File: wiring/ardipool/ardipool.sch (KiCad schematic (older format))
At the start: 23 parts, among them K1 filter, K2 ph, P1 Digital, P10 CONN_01X01, P11 CONN_01X01, P12 CONN_01X01, P13 CONN_01X01, P2 Power, P3 Analog, P4 Analog, P5 PWM, P6 PWM, P7 Communication, P8 CONN_01X01, P9 CONN_01X01, SW1 SW_Push_Dual, U1 DS18B20, U2 DS18B20, U3 DHT11, U4 DS1307+

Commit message: schem
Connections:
- net 6(**) is gone; now on net LCD5: P6.2 (Pin_2)
- net 7(**) is gone; now on net LCD4: P6.1 (Pin_1)
- net LCD4: no longer P6.3 (Pin_3)
- net LCD5: no longer P6.4 (Pin_4)
- net LCD6: now also P6.3 (Pin_3); no longer P6.5 (Pin_5)
- net LCD7: now also P6.4 (Pin_4); no longer P6.6 (Pin_6)
- net 18(Tx1) renamed Rotary2
- net 19(Rx1) renamed Rotary1
- new net 3(**): P6.5 (Pin_5)
- new net RotaryB: P6.6 (Pin_6)
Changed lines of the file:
@@
 	8900 3150 9350 3150
 Wire Wire Line
-	10400 2450 10150 2450
-Wire Wire Line
-	10150 2550 10400 2550
-Wire Wire Line
 	10400 3050 10150 3050
 Wire Wire Line
@@
 Wire Wire Line
 	10150 3700 10400 3700
-Wire Wire Line
-	10400 3800 10150 3800
-Wire Wire Line
-	10150 3900 10400 3900
-Wire Wire Line
-	10400 4000 10150 4000
-Wire Wire Line
-	10150 4100 10400 4100
 Wire Wire Line
 	10500 4850 10500 4650
@@
 	1    0    0    -1
 $EndComp
-Text GLabel 10400 4000 2    50   Input ~ 0
+Text GLabel 10850 4000 2    50   Input ~ 0
 SDA
-Text GLabel 10400 4100 2    50   Input ~ 0
+Text GLabel 10850 4100 2    50   Input ~ 0
 SCL
 Wire Wire Line
@@
 Wire Wire Line
 	6050 5850 6300 5850
-Text GLabel 10700 2650 2    50   Input ~ 0
+Text GLabel 10850 2450 2    50   Input ~ 0
 LCD4
-Text GLabel 10700 2750 2    50   Input ~ 0
+Text GLabel 10850 2550 2    50   Input ~ 0
 LCD5
-Text GLabel 10700 2850 2    50   Input ~ 0
+Text GLabel 10850 2650 2    50   Input ~ 0
 LCD6
-Text GLabel 10700 2950 2    50   Input ~ 0
+Text GLabel 10850 2750 2    50   Input ~ 0
 LCD7
 Wire Wire Line
-	10150 2650 10700 2650
-Wire Wire Line
-	10150 2750 10700 2750
-Wire Wire Line
 	10150 2850 10700 2850
-Wire Wire Line
-	10150 2950 10700 2950
 Text GLabel 10850 1650 2    50   Input ~ 0
 LCDRS
@@
 Wire Wire Line
 	3250 4000 3250 3900
+Wire Wire Line
+	10150 2450 10850 2450
+Wire Wire Line
+	10150 2550 10850 2550
+Wire Wire Line
+	10150 2650 10850 2650
+Wire Wire Line
+	10150 2750 10850 2750
+Wire Wire Line
+	10150 4000 10850 4000
+Wire Wire Line
+	10150 4100 10850 4100
+Text GLabel 10850 3900 2    50   Input ~ 0
+Rotary1
+Text GLabel 10850 3800 2    50   Input ~ 0
+Rotary2
+Text GLabel 10850 2950 2    50   Input ~ 0
+RotaryB
+Wire Wire Line
+	10150 2950 10850 2950
+Wire Wire Line
+	10150 3800 10850 3800
+Wire Wire Line
+	10150 3900 10850 3900
 $EndSCHEMATC

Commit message: update network
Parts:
- added U?: devkitC, symbol arduitouch:devkitC
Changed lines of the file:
@@
 Wire Wire Line
 	10150 3900 10850 3900
+Text GLabel 1350 950  0    50   Input ~ 0
+12V
+Text GLabel 1350 1100 0    50   Input ~ 0
+GND
+Text GLabel 1350 1250 0    50   Input ~ 0
+Relay1
+Text GLabel 1350 1400 0    50   Input ~ 0
+Relay2
+Text GLabel 1350 1550 0    50   Input ~ 0
+Relay3
+Text GLabel 1350 1700 0    50   Input ~ 0
+Relay3
+Text GLabel 1350 1850 0    50   Input ~ 0
+DS18B20
+Text GLabel 1350 800  0    50   Input ~ 0
+3.3V
+Text GLabel 1350 2000 0    50   Input ~ 0
+SCA
+Text GLabel 1350 2150 0    50   Input ~ 0
+SCL
+$Comp
+L arduitouch:devkitC U?
+U 1 1 5F01B682
+P 2650 1150
+F 0 "U?" H 3269 826 50  0000 L CNN
+F 1 "devkitC" H 3269 735 50  0000 L CNN
+F 2 "" H 2650 1150 50  0001 C CNN
+F 3 "" H 2650 1150 50  0001 C CNN
+	1    2650 1150
+	1    0    0    -1
+$EndComp
 $EndSCHEMATC

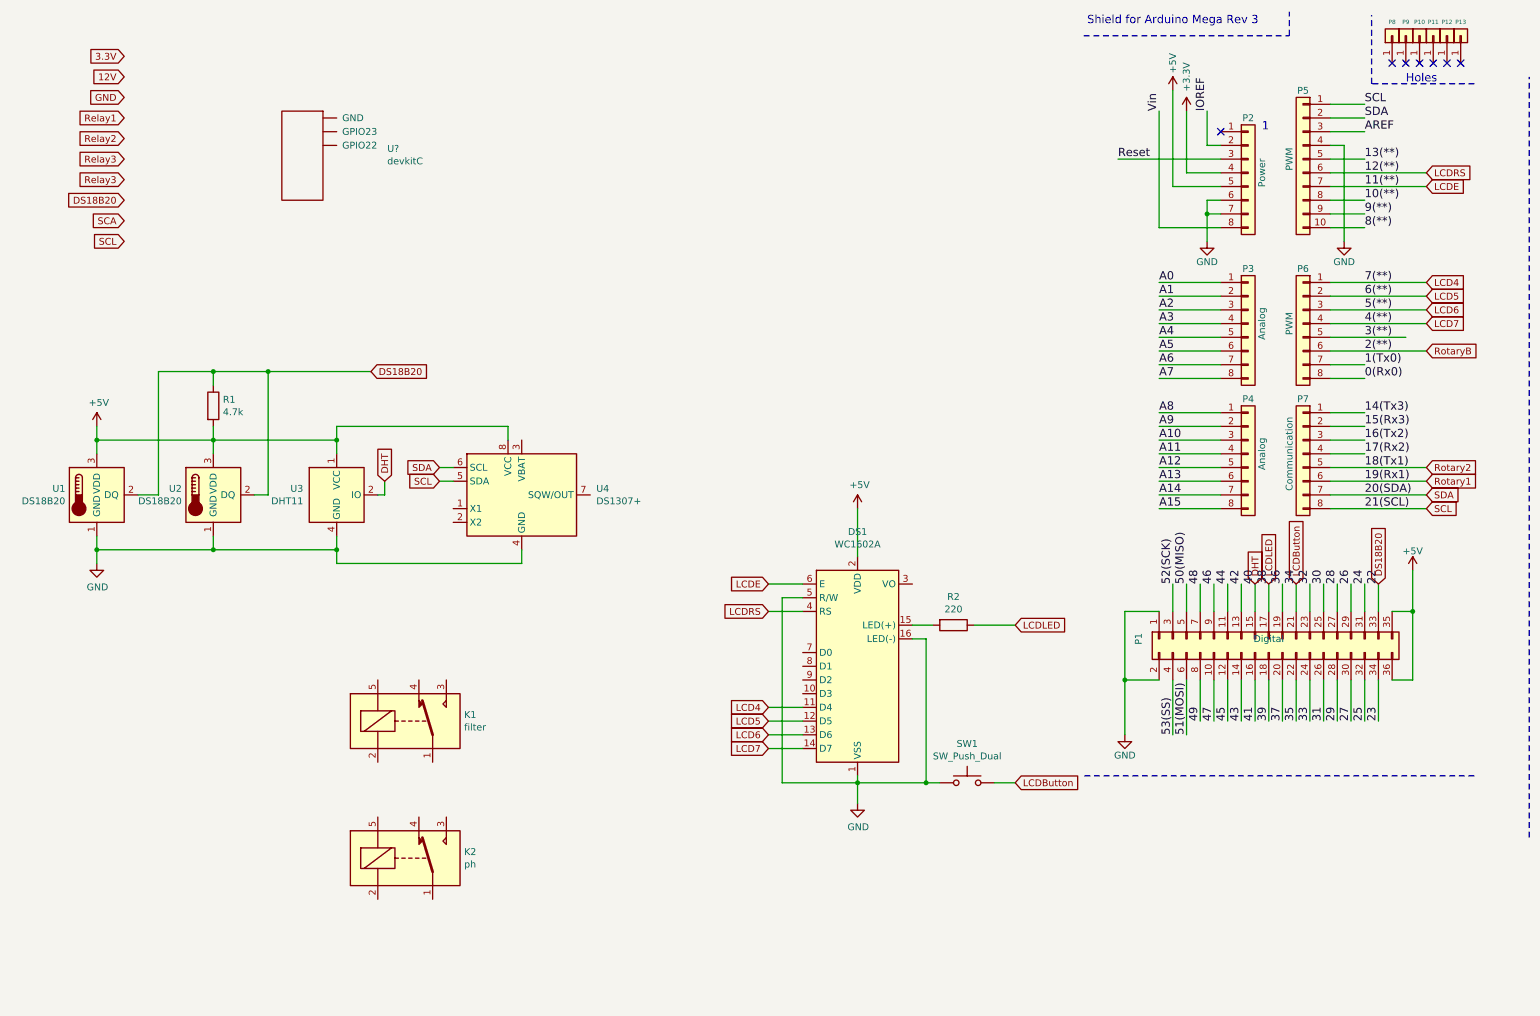
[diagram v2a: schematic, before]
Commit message: make use of config.states
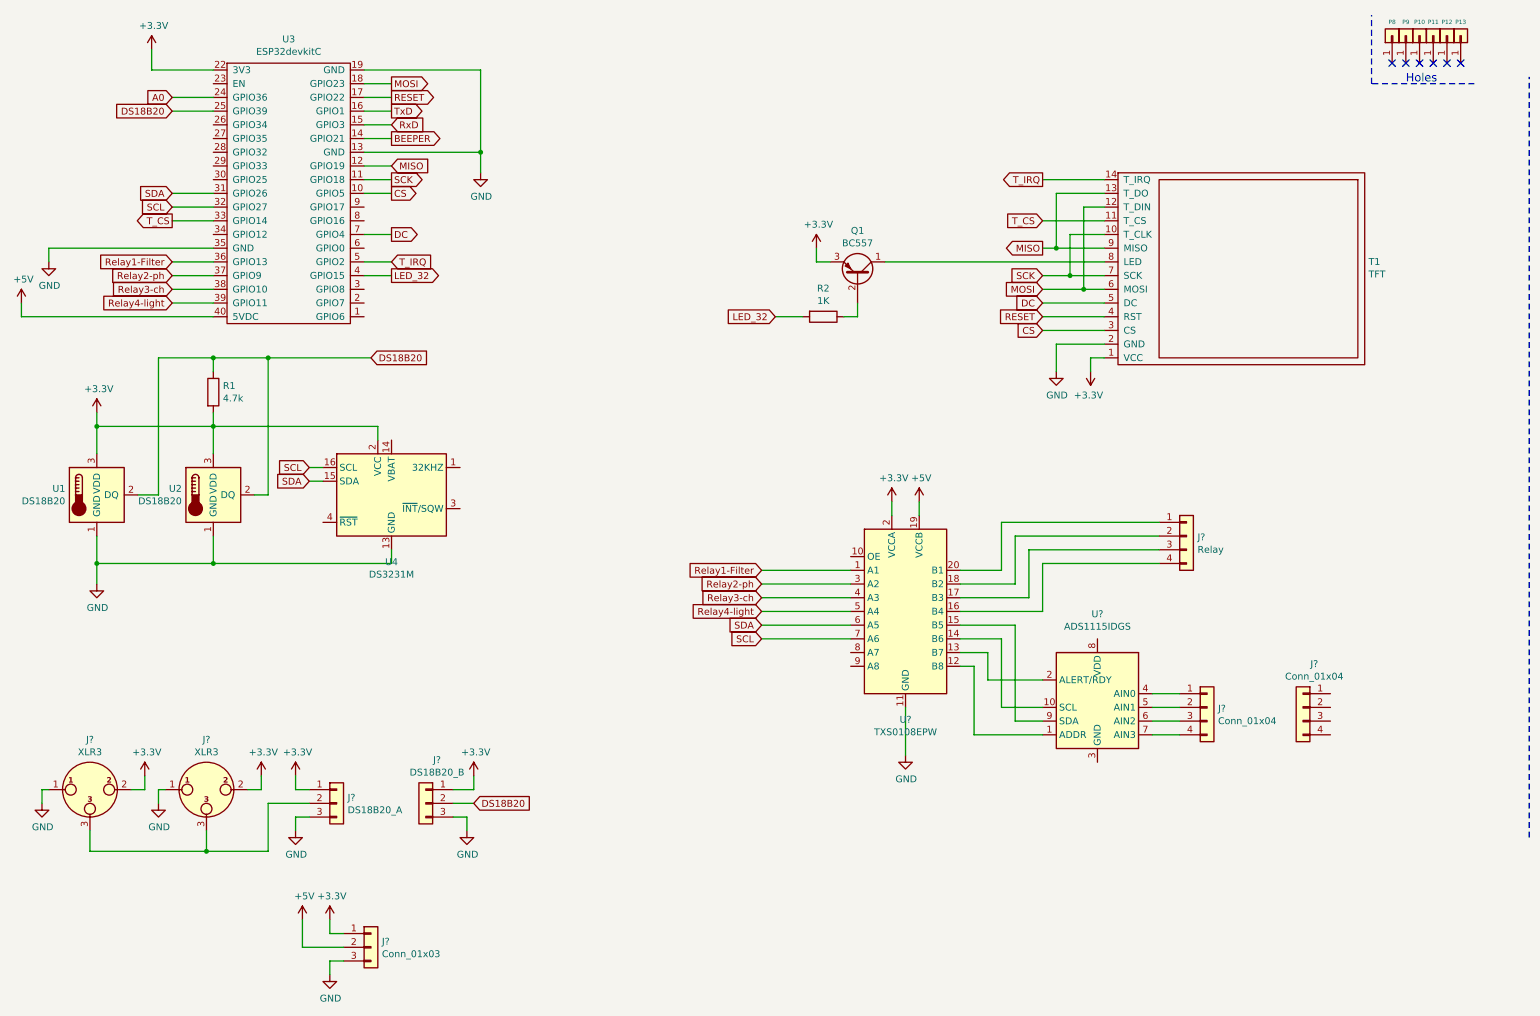
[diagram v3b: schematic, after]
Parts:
- removed DS1: WC1602A, Display:WC1602A, symbol Display_Character:WC1602A
- removed K1: filter, Relay_THT:Relay_SPDT_SANYOU_SRD_Series_Form_C, symbol Relay:SANYOU_SRD_Form_C
- removed K2: ph, Relay_THT:Relay_SPDT_SANYOU_SRD_Series_Form_C, symbol Relay:SANYOU_SRD_Form_C
- removed P1: Digital, Socket_Arduino_Mega:Socket_Strip_Arduino_2x18, symbol Connector_Generic:Conn_02x18_Odd_Even
- removed P2: Power, Socket_Arduino_Mega:Socket_Strip_Arduino_1x08, symbol Connector_Generic:Conn_01x08
- removed P3, P4: Analog, Socket_Arduino_Mega:Socket_Strip_Arduino_1x08, symbol Connector_Generic:Conn_01x08
- removed P5: PWM, Socket_Arduino_Mega:Socket_Strip_Arduino_1x10, symbol Connector_Generic:Conn_01x10
- removed P6: PWM, Socket_Arduino_Mega:Socket_Strip_Arduino_1x08, symbol Connector_Generic:Conn_01x08
- removed P7: Communication, Socket_Arduino_Mega:Socket_Strip_Arduino_1x08, symbol Connector_Generic:Conn_01x08
- removed SW1: SW_Push_Dual, Button_Switch_THT:SW_PUSH_6mm_H5mm, symbol Switch:SW_Push
- removed U3: DHT11, Sensor:Aosong_DHT11_5.5x12.0_P2.54mm, symbol Sensor:DHT11
- removed U4: DS1307+, Package_DIP:DIP-8_W7.62mm, symbol Timer_RTC:DS1307+
- removed U?: devkitC, symbol arduitouch:devkitC
- added J? (x2): XLR3, symbol Connector:XLR3
- added J?: Relay, symbol Connector_Generic:Conn_01x04
- added J? (x2): Conn_01x04, symbol Connector_Generic:Conn_01x04
- added J?: DS18B20_A, symbol Connector_Generic:Conn_01x03
- added J?: Conn_01x03, symbol Connector_Generic:Conn_01x03
- added J?: DS18B20_B, symbol Connector_Generic:Conn_01x03
- added Q1: BC557, Package_TO_SOT_THT:TO-92_Inline_Wide, symbol Transistor_BJT:BC557
- added T1: TFT, symbol arduitouch:TFT
- added U3: ESP32devkitC, symbol arduitouch:ESP32devkitC
- added U4: DS3231M, Package_SO:SOIC-16W_7.5x10.3mm_P1.27mm, symbol Timer_RTC:DS3231M
- added U?: TXS0108EPW, Package_SO:TSSOP-20_4.4x6.5mm_P0.65mm, symbol Logic_LevelTranslator:TXS0108EPW
- added U?: ADS1115IDGS, Package_SO:TSSOP-10_3x3mm_P0.5mm, symbol Analog_ADC:ADS1115IDGS
- R2: value 220 -> 1K; footprint Resistor_THT:R_Axial_DIN0207_L6.3mm_D2.5mm_P10.16mm_Horizontal -> (none)
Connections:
- net +3V3: now also R1.2, U1.3 (VDD), U2.3 (VDD), J?.1 (Pin_1), J?.1 (Pin_1), J?.1 (Pin_1), J?.2, J?.2, Q1.3 (E), T1.1 (VCC), U3.22 (3V3), U4.2 (VCC), U?.2 (VCCA)
- net +5V: now also J?.2 (Pin_2), U3.40 (5VDC), U?.19 (VCCB); no longer R1.2, U1.3 (VDD), U2.3 (VDD)
- net A0: now also U3.24 (GPIO36)
- net DS18B20: now also J?.2 (Pin_2), U3.25 (GPIO39)
- net GND: now also J?.1, J?.1, J?.3 (Pin_3), J?.3 (Pin_3), J?.3 (Pin_3), T1.2 (GND), U3.13 (GND), U3.19 (GND), U3.35 (GND), U4.10 (GND), U4.11 (GND), U4.12 (GND), U4.13 (GND), U4.5 (GND), U4.6 (GND), U4.7 (GND), U4.8 (GND), U4.9 (GND), U?.11 (GND)
- net SCL: now also U3.32 (GPIO27), U4.16 (SCL), U?.7 (A6)
- net SDA: now also U3.31 (GPIO26), U4.15 (SDA), U?.6 (A5)
- net LED_32: now reaches R2.2
- net LED_32: now also U3.4 (GPIO15)
- net LCDLED: no longer names the net of R2.1
- net LCDLED: now also Q1.2 (B)
- new net: Q1.1 (C), T1.8 (LED)
- new net: J?.2 (Pin_2), J?.3, J?.3
- new net: J?.1 (Pin_1), U?.20 (B1)
- new net: J?.2 (Pin_2), U?.18 (B2)
- new net: J?.3 (Pin_3), U?.17 (B3)
- new net: J?.4 (Pin_4), U?.16 (B4)
- new net: J?.1 (Pin_1), U?.4 (AIN0)
- new net: J?.2 (Pin_2), U?.5 (AIN1)
- new net: J?.3 (Pin_3), U?.6 (AIN2)
- new net: J?.4 (Pin_4), U?.7 (AIN3)
- new net: U?.1 (ADDR), U?.12 (B8)
- new net: U?.13 (B7), U?.2 (ALERT/RDY)
- new net: U?.10 (SCL), U?.14 (B6)
- new net: U?.15 (B5), U?.9 (SDA)
- new net BEEPER: U3.14 (GPIO21)
- new net CS: T1.3 (CS), U3.10 (GPIO5)
- new net DC: T1.5 (DC), U3.7 (GPIO4)
- new net MISO: T1.13 (T_DO), T1.9 (MISO), U3.12 (GPIO19)
- new net MOSI: T1.12 (T_DIN), T1.6 (MOSI), U3.18 (GPIO23)
- new net RESET: T1.4 (RST), U3.17 (GPIO22)
- new net Relay1-Filter: U3.36 (GPIO13), U?.1 (A1)
- new net Relay2-ph: U3.37 (GPIO9), U?.3 (A2)
- new net Relay3-ch: U3.38 (GPIO10), U?.4 (A3)
- new net Relay4-light: U3.39 (GPIO11), U?.5 (A4)
- new net RxD: U3.15 (GPIO3)
- new net SCK: T1.10 (T_CLK), T1.7 (SCK), U3.11 (GPIO18)
- new net T_CS: T1.11 (T_CS), U3.33 (GPIO14)
- new net T_IRQ: T1.14 (T_IRQ), U3.5 (GPIO2)
- new net TxD: U3.16 (GPIO1)
- no-connect marks 7 -> 6
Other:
- note removed: "1"
- note removed: "Shield for Arduino Mega Rev 3"
- moved on the sheet: R1

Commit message: update
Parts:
- removed J?: Relay, symbol Connector_Generic:Conn_01x04
- removed J?: Conn_01x04, symbol Connector_Generic:Conn_01x04
- removed U?: TXS0108EPW, Package_SO:TSSOP-20_4.4x6.5mm_P0.65mm, symbol Logic_LevelTranslator:TXS0108EPW
- removed U?: ADS1115IDGS, Package_SO:TSSOP-10_3x3mm_P0.5mm, symbol Analog_ADC:ADS1115IDGS
- U3: footprint (none) -> Package_DIP:DIP-40_W25.4mm_Socket_LongPads
- gave numbers to parts that had none: 6

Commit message: feat: Working without pressure
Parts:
- R1: value 4.7k -> 2.7k
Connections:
- net DS18B20: now also U3.30 (GPIO25); no longer U3.25 (GPIO39)
- net Relay2-ph: now also U3.28 (GPIO32); no longer U3.37 (GPIO9)
- net Relay3-ch: now also U3.29 (GPIO33); no longer U3.38 (GPIO10)
- net Relay4-light: now also U3.8 (GPIO16); no longer U3.39 (GPIO11)
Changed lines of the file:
@@
 P 2000 3250
 F 0 "R1" H 2070 3296 50  0000 L CNN
-F 1 "4.7k" H 2070 3205 50  0000 L CNN
+F 1 "2.7k" H 2070 3205 50  0000 L CNN
 F 2 "Resistor_THT:R_Axial_DIN0207_L6.3mm_D2.5mm_P10.16mm_Horizontal" V 1930 3250 50  0001 C CNN
 F 3 "~" H 2000 3250 50  0001 C CNN
@@
 Text GLabel 2700 3800 0    50   Input ~ 0
 SCL
-Text GLabel 1700 2300 0    50   Input ~ 0
+Text GLabel 1700 2300 0    50   Output ~ 0
 Relay1-Filter
-Text GLabel 1700 2400 0    50   Input ~ 0
+Text GLabel 1700 1500 0    50   Output ~ 0
 Relay2-ph
-Text GLabel 1700 2500 0    50   Input ~ 0
+Text GLabel 1700 1600 0    50   Output ~ 0
 Relay3-ch
-Text GLabel 1700 2600 0    50   Input ~ 0
+Text GLabel 3300 2000 2    50   Output ~ 0
 Relay4-light
-Text GLabel 1700 1200 0    50   Input ~ 0
+Text GLabel 1700 1700 0    50   Input ~ 0
 DS18B20
 Text GLabel 1700 1800 0    50   Input ~ 0
@@
 Wire Wire Line
 	1700 2300 2000 2300
-Wire Wire Line
-	1700 2400 2000 2400
-Wire Wire Line
-	1700 2500 2000 2500
-Wire Wire Line
-	1700 2600 2000 2600
 $Comp
 L power:+3.3V #PWR0101
@@
 Wire Wire Line
 	1700 1100 2000 1100
-Wire Wire Line
-	2000 1200 1700 1200
 $Comp
 L arduitouch:TFT T1
@@
 F1 "extensionBoard.sch" 50
 $EndSheet
+Wire Wire Line
+	1700 1700 2000 1700
+Wire Wire Line
+	1700 2100 2000 2100
+Wire Wire Line
+	3100 2000 3300 2000
+Wire Wire Line
+	1700 1600 2000 1600
+Wire Wire Line
+	1700 1500 2000 1500
 $EndSCHEMATC
